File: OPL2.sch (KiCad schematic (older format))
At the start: 8 parts, among them J1 Conn_01x08_Male, U1 LM358, U2 YM3014B, U3 YM3812, U4 PROMINI

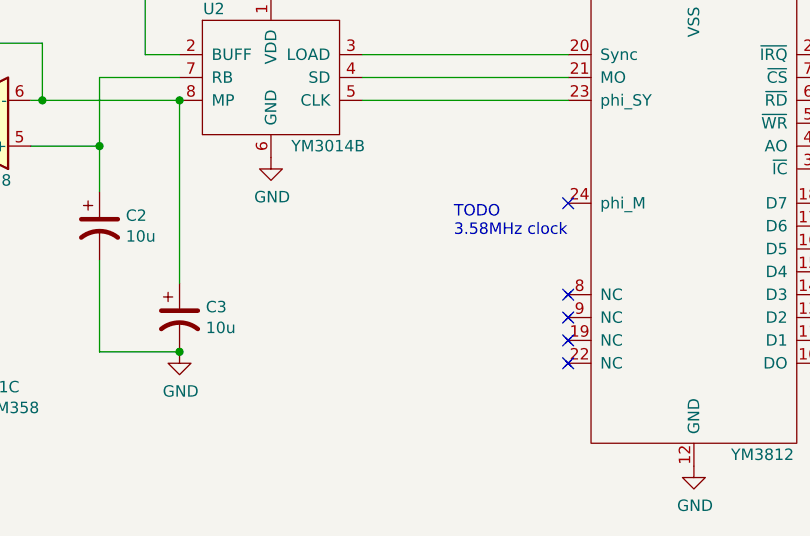
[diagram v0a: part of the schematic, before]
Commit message: add footprints to everything; add header for clock subcircuit
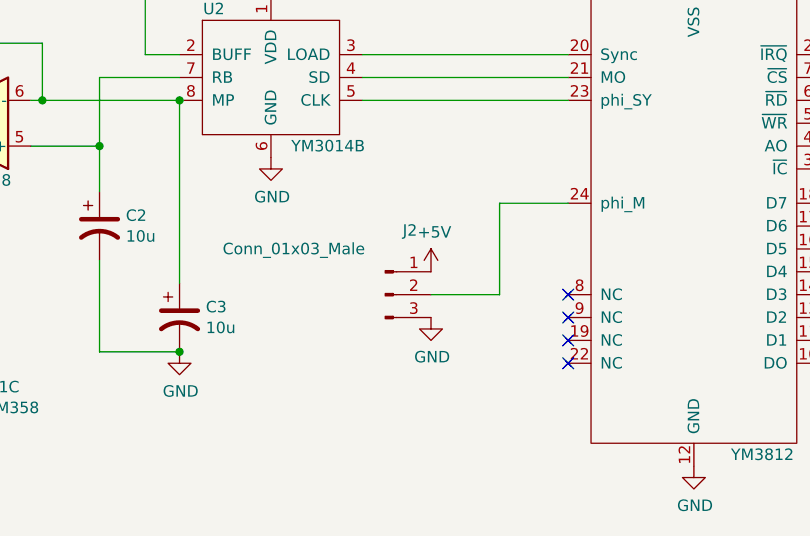
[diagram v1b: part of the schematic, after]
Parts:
- added J2: Conn_01x03_Male, Connector_PinHeader_2.54mm:PinHeader_1x03_P2.54mm_Vertical, symbol Connector:Conn_01x03_Male
- C1, C2, C3: footprint (none) -> Capacitor_THT:CP_Radial_D7.5mm_P2.50mm
- J1: footprint (none) -> Connector_PinHeader_2.54mm:PinHeader_1x08_P2.54mm_Vertical
- U1, U2: footprint (none) -> Package_DIP:DIP-8_W7.62mm_LongPads
- U3, U4: footprint (none) -> Package_DIP:DIP-24_W15.24mm_LongPads
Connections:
- net +5V: now also J2.1 (Pin_1)
- net GND: now also J2.3 (Pin_3)
- net at U3.24 (phi_M): now also J2.2 (Pin_2)
- no-connect marks 12 -> 11
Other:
- note removed: "TODO\n3.58MHz clock"
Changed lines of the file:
@@
 F 0 "U3" H 6050 4750 50  0000 C CNN
 F 1 "YM3812" H 6750 2700 50  0000 C CNN
-F 2 "" H 6000 4750 50  0001 C CNN
+F 2 "Package_DIP:DIP-24_W15.24mm_LongPads" H 6000 4750 50  0001 C CNN
 F 3 "" H 6000 4750 50  0001 C CNN
 	1    6450 3800
@@
 F 0 "U2" H 4350 3550 50  0000 C CNN
 F 1 "YM3014B" H 4850 2950 50  0000 C CNN
-F 2 "" H 4300 3550 50  0001 C CNN
+F 2 "Package_DIP:DIP-8_W7.62mm_LongPads" H 4300 3550 50  0001 C CNN
 F 3 "" H 4300 3550 50  0001 C CNN
 	1    4600 3250
@@
 F 0 "U1" H 3250 2917 50  0000 C CNN
 F 1 "LM358" H 3250 2826 50  0000 C CNN
-F 2 "" H 3250 2550 50  0001 C CNN
+F 2 "Package_DIP:DIP-8_W7.62mm_LongPads" H 3250 2550 50  0001 C CNN
 F 3 "http://www.ti.com/lit/ds/symlink/lm2904-n.pdf" H 3250 2550 50  0001 C CNN
 	1    3250 2550
@@
 F 0 "U1" H 3400 3300 50  0000 C CNN
 F 1 "LM358" H 3150 3700 50  0000 C CNN
-F 2 "" H 3250 3450 50  0001 C CNN
+F 2 "Package_DIP:DIP-8_W7.62mm_LongPads" H 3250 3450 50  0001 C CNN
 F 3 "http://www.ti.com/lit/ds/symlink/lm2904-n.pdf" H 3250 3450 50  0001 C CNN
 	2    3250 3450
@@
 F 0 "U1" H 3358 4696 50  0000 L CNN
 F 1 "LM358" H 3358 4605 50  0000 L CNN
-F 2 "" H 3400 4650 50  0001 C CNN
+F 2 "Package_DIP:DIP-8_W7.62mm_LongPads" H 3400 4650 50  0001 C CNN
 F 3 "http://www.ti.com/lit/ds/symlink/lm2904-n.pdf" H 3400 4650 50  0001 C CNN
 	3    3400 4650
@@
 F 0 "U4" H 8700 4150 50  0000 C CNN
 F 1 "PROMINI" H 9400 2750 50  0000 C CNN
-F 2 "" H 9000 3700 50  0001 C CNN
+F 2 "Package_DIP:DIP-24_W15.24mm_LongPads" H 9000 3700 50  0001 C CNN
 F 3 "" H 9000 3700 50  0001 C CNN
 	1    9100 3700
@@
 F 0 "J1" H 9308 2231 50  0000 C CNN
 F 1 "Conn_01x08_Male" H 8900 2150 50  0000 C CNN
-F 2 "" H 9200 1750 50  0001 C CNN
+F 2 "Connector_PinHeader_2.54mm:PinHeader_1x08_P2.54mm_Vertical" H 9200 1750 50  0001 C CNN
 F 3 "~" H 9200 1750 50  0001 C CNN
 	1    9200 1750
@@
 F 0 "C2" H 3965 3946 50  0000 L CNN
 F 1 "10u" H 3965 3855 50  0000 L CNN
-F 2 "" H 3850 3900 50  0001 C CNN
+F 2 "Capacitor_THT:CP_Radial_D7.5mm_P2.50mm" H 3850 3900 50  0001 C CNN
 F 3 "~" H 3850 3900 50  0001 C CNN
 	1    3850 3900
@@
 F 0 "C3" H 4315 4346 50  0000 L CNN
 F 1 "10u" H 4315 4255 50  0000 L CNN
-F 2 "" H 4200 4300 50  0001 C CNN
+F 2 "Capacitor_THT:CP_Radial_D7.5mm_P2.50mm" H 4200 4300 50  0001 C CNN
 F 3 "~" H 4200 4300 50  0001 C CNN
 	1    4200 4300
@@
 F 0 "C1" H 3015 4696 50  0000 L CNN
 F 1 "100n" H 3015 4605 50  0000 L CNN
-F 2 "" H 2938 4500 50  0001 C CNN
+F 2 "Capacitor_THT:CP_Radial_D7.5mm_P2.50mm" H 2938 4500 50  0001 C CNN
 F 3 "~" H 2900 4650 50  0001 C CNN
 	1    2900 4650
@@
 	1    0    0    -1
 $EndComp
-NoConn ~ 5900 3800
-Text Notes 5400 3950 0    50   ~ 0
-TODO\n3.58MHz clock
+$Comp
+L Connector:Conn_01x03_Male J2
+U 1 1 610B5902
+P 5100 4200
+F 0 "J2" H 5208 4481 50  0000 C CNN
+F 1 "Conn_01x03_Male" H 4700 4400 50  0000 C CNN
+F 2 "Connector_PinHeader_2.54mm:PinHeader_1x03_P2.54mm_Vertical" H 5100 4200 50  0001 C CNN
+F 3 "~" H 5100 4200 50  0001 C CNN
+	1    5100 4200
+	1    0    0    -1
+$EndComp
+Wire Wire Line
+	5900 3800 5600 3800
+Wire Wire Line
+	5600 3800 5600 4200
+Wire Wire Line
+	5600 4200 5300 4200
+$Comp
+L power:GND #PWR0116
+U 1 1 610BC6EB
+P 5300 4300
+F 0 "#PWR0116" H 5300 4050 50  0001 C CNN
+F 1 "GND" H 5305 4127 50  0000 C CNN
+F 2 "" H 5300 4300 50  0001 C CNN
+F 3 "" H 5300 4300 50  0001 C CNN
+	1    5300 4300
+	1    0    0    -1
+$EndComp
+$Comp
+L power:+5V #PWR0117
+U 1 1 610BCE38
+P 5300 4100
+F 0 "#PWR0117" H 5300 3950 50  0001 C CNN
+F 1 "+5V" H 5315 4273 50  0000 C CNN
+F 2 "" H 5300 4100 50  0001 C CNN
+F 3 "" H 5300 4100 50  0001 C CNN
+	1    5300 4100
+	1    0    0    -1
+$EndComp
 $EndSCHEMATC
